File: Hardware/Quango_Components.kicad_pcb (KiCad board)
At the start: 4 copper layers, 70.6 x 100 mm, 175 parts, among them J1 Conn_01x12_Male, J2 Conn_01x12_Male, J3 Conn_01x12_Male, J4 Conn_01x12_Male, J5 SWD_Header, J6 Eurorack_10_pin_power, J7 Audio_Breakout, Q1 MMBT3904, U1 LM1117-3.3, U10 TL074, U11 TL074, U12 TL074, U13 TL074, U14 TL074, U2 STM32G473V, U3 LM1117-5.0, U4 PS508, U5 MCP6002, U6 AS3364, U7 AS3364, U8 AD5676, U9 MCP48CMB21, Y1 8MHz 20pF

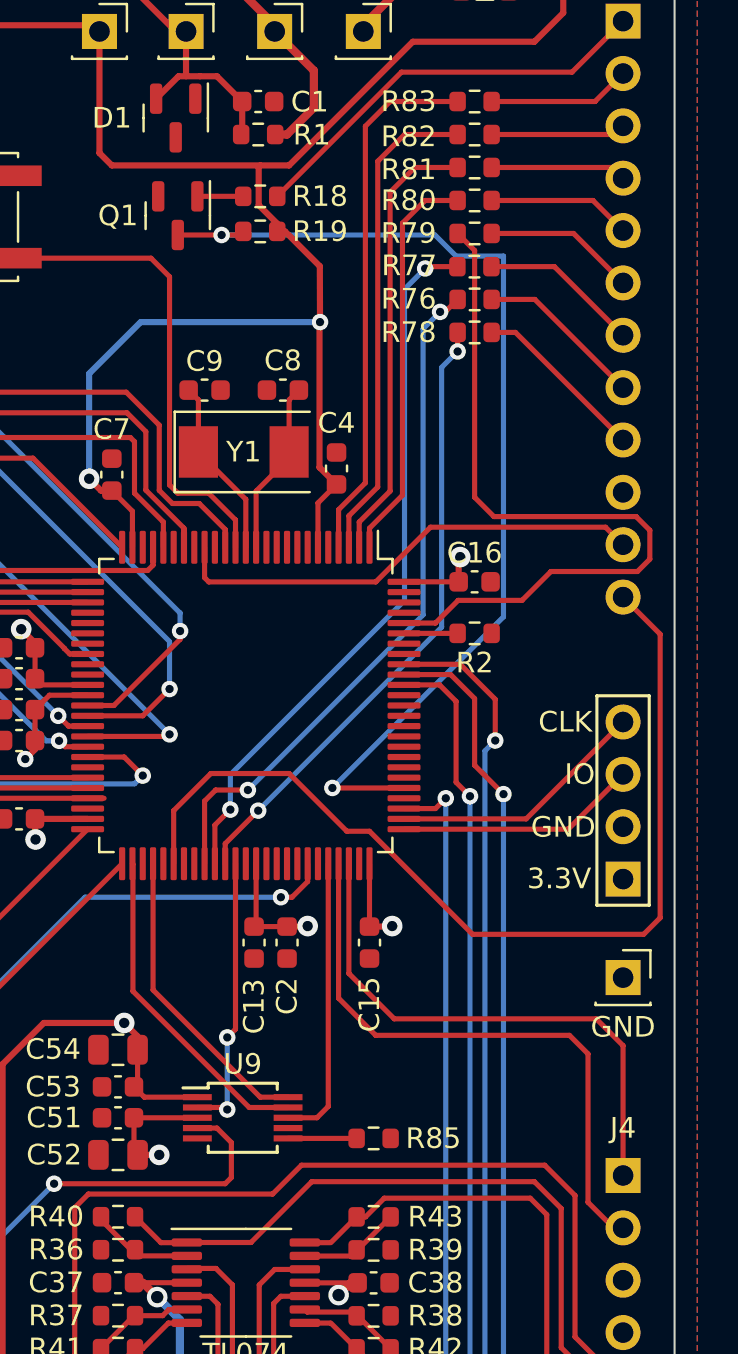
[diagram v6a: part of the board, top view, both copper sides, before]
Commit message: First draft routing of control board
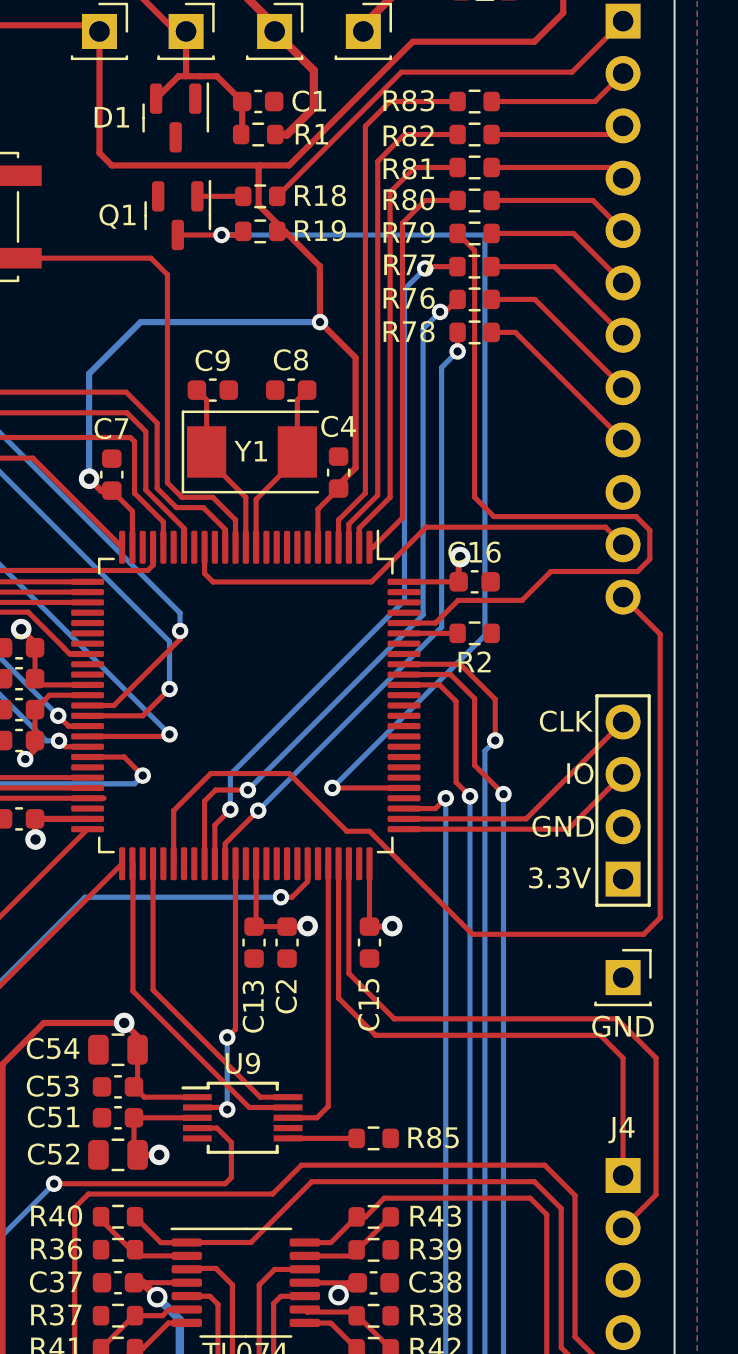
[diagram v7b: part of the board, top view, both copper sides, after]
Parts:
- moved Y1 0.40 mm to (100.2, 72.9)
- moved C8 0.40 mm to (102.1, 69.9)
- moved C9 0.40 mm to (98.3, 69.9)
- moved C4 0.22 mm to (104.4, 73.9)
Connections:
- J3 pad 2: /EnvB4_LED_Out -> /EnvA4_LED_Out
- J3 pad 3: /EnvB3_LED_Out -> /EnvA3_LED_Out
- J3 pad 4: /EnvB2_LED_Out -> /EnvA2_LED_Out
- J3 pad 5: /EnvB1_LED_Out -> /EnvA1_LED_Out
- J3 pad 6: /EnvA4_LED_Out -> /EnvB4_LED_Out
- J3 pad 7: /EnvA2_LED_Out -> /EnvB2_LED_Out
- J3 pad 8: /EnvA1_LED_Out -> /EnvB1_LED_Out
- J3 pad 9: /EnvA3_LED_Out -> /EnvB3_LED_Out
- J4 pad 1: /USB_DP -> /USB_DM
- J4 pad 2: /USB_DM -> /USB_DP
- R76 pad 1: /EnvA1_LED_Out -> /EnvB1_LED_Out
- R76 pad 2: /EnvA1_LED -> /EnvB1_LED
- R77 pad 1: /EnvA2_LED_Out -> /EnvB2_LED_Out
- R77 pad 2: /EnvA2_LED -> /EnvB2_LED
- R78 pad 1: /EnvA3_LED_Out -> /EnvB3_LED_Out
- R78 pad 2: /EnvA3_LED -> /EnvB3_LED
- R79 pad 1: /EnvA4_LED_Out -> /EnvB4_LED_Out
- R79 pad 2: /EnvA4_LED -> /EnvB4_LED
- R80 pad 1: /EnvB1_LED_Out -> /EnvA1_LED_Out
- R80 pad 2: /EnvB1_LED -> /EnvA1_LED
- R81 pad 1: /EnvB2_LED_Out -> /EnvA2_LED_Out
- R81 pad 2: /EnvB2_LED -> /EnvA2_LED
- R82 pad 1: /EnvB3_LED_Out -> /EnvA3_LED_Out
- R82 pad 2: /EnvB3_LED -> /EnvA3_LED
- R83 pad 1: /EnvB4_LED_Out -> /EnvA4_LED_Out
- R83 pad 2: /EnvB4_LED -> /EnvA4_LED
- U2 pad 1: /EnvB1_LED -> /EnvA1_LED
- U2 pad 2: /EnvB2_LED -> /EnvA2_LED
- U2 pad 3: /EnvB3_LED -> /EnvA3_LED
- U2 pad 4: /EnvB4_LED -> /EnvA4_LED
- U2 pad 59: /EnvA1_LED -> /EnvB1_LED
- U2 pad 60: /EnvA2_LED -> /EnvB2_LED
- U2 pad 61: /EnvA3_LED -> /EnvB3_LED
- U2 pad 96: /EnvA4_LED -> /EnvB4_LED
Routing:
- net /EnvB1_LED: track 19.5 -> 33.5 mm, vias 0 -> 2
- net /EnvA1_LED: track 33.5 -> 19.6 mm, vias 2 -> 0
- net /EnvB2_LED: track 21.6 -> 34.7 mm, vias 0 -> 2
- net /EnvA2_LED: track 34.7 -> 21.6 mm, vias 2 -> 0
- net /EnvB4_LED: track 25.9 -> 36.9 mm
- net /EnvA4_LED: track 36.9 -> 25.9 mm
- net /EnvB3_LED: track 23.7 -> 30.4 mm, vias 0 -> 2
- net /EnvA3_LED: track 30.4 -> 23.7 mm, vias 2 -> 0
- net /USB_DP: track 26.4 -> 31.3 mm
- net /EnvB3_LED_Out: track 6.55 -> 8.54 mm
- net /EnvA3_LED_Out: track 8.54 -> 6.55 mm
- net /USB_DM: track 29.2 -> 27.2 mm
- net /EnvB2_LED_Out: track 6.59 -> 7.76 mm
- net /EnvA2_LED_Out: track 7.76 -> 6.59 mm
- net /EnvB1_LED_Out: track 6.98 -> 8.15 mm
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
